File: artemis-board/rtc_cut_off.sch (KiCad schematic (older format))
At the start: 10 parts, among them Q1 2N7002, Q3 2N7002, U7 PCF8563T, U9 TCA6408A, Y2 32.768KHz

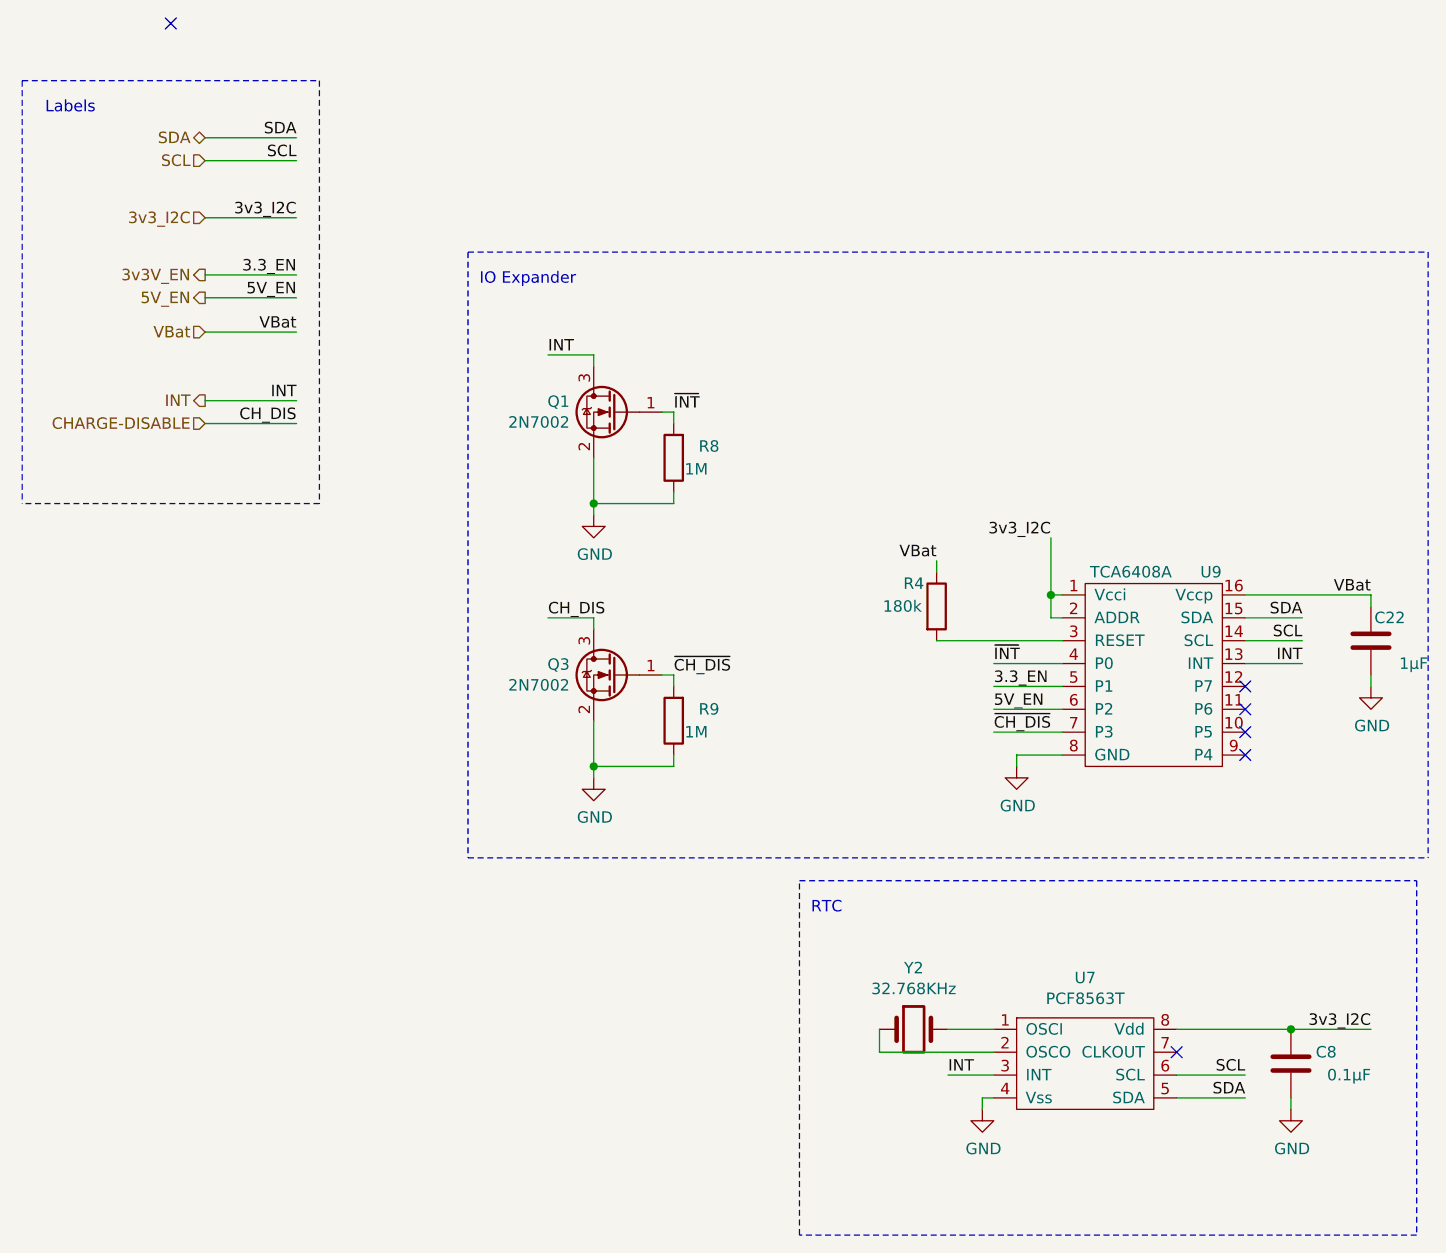
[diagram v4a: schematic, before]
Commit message: added cirquit to measure Vbat with esp in case of fuel gauge shortage
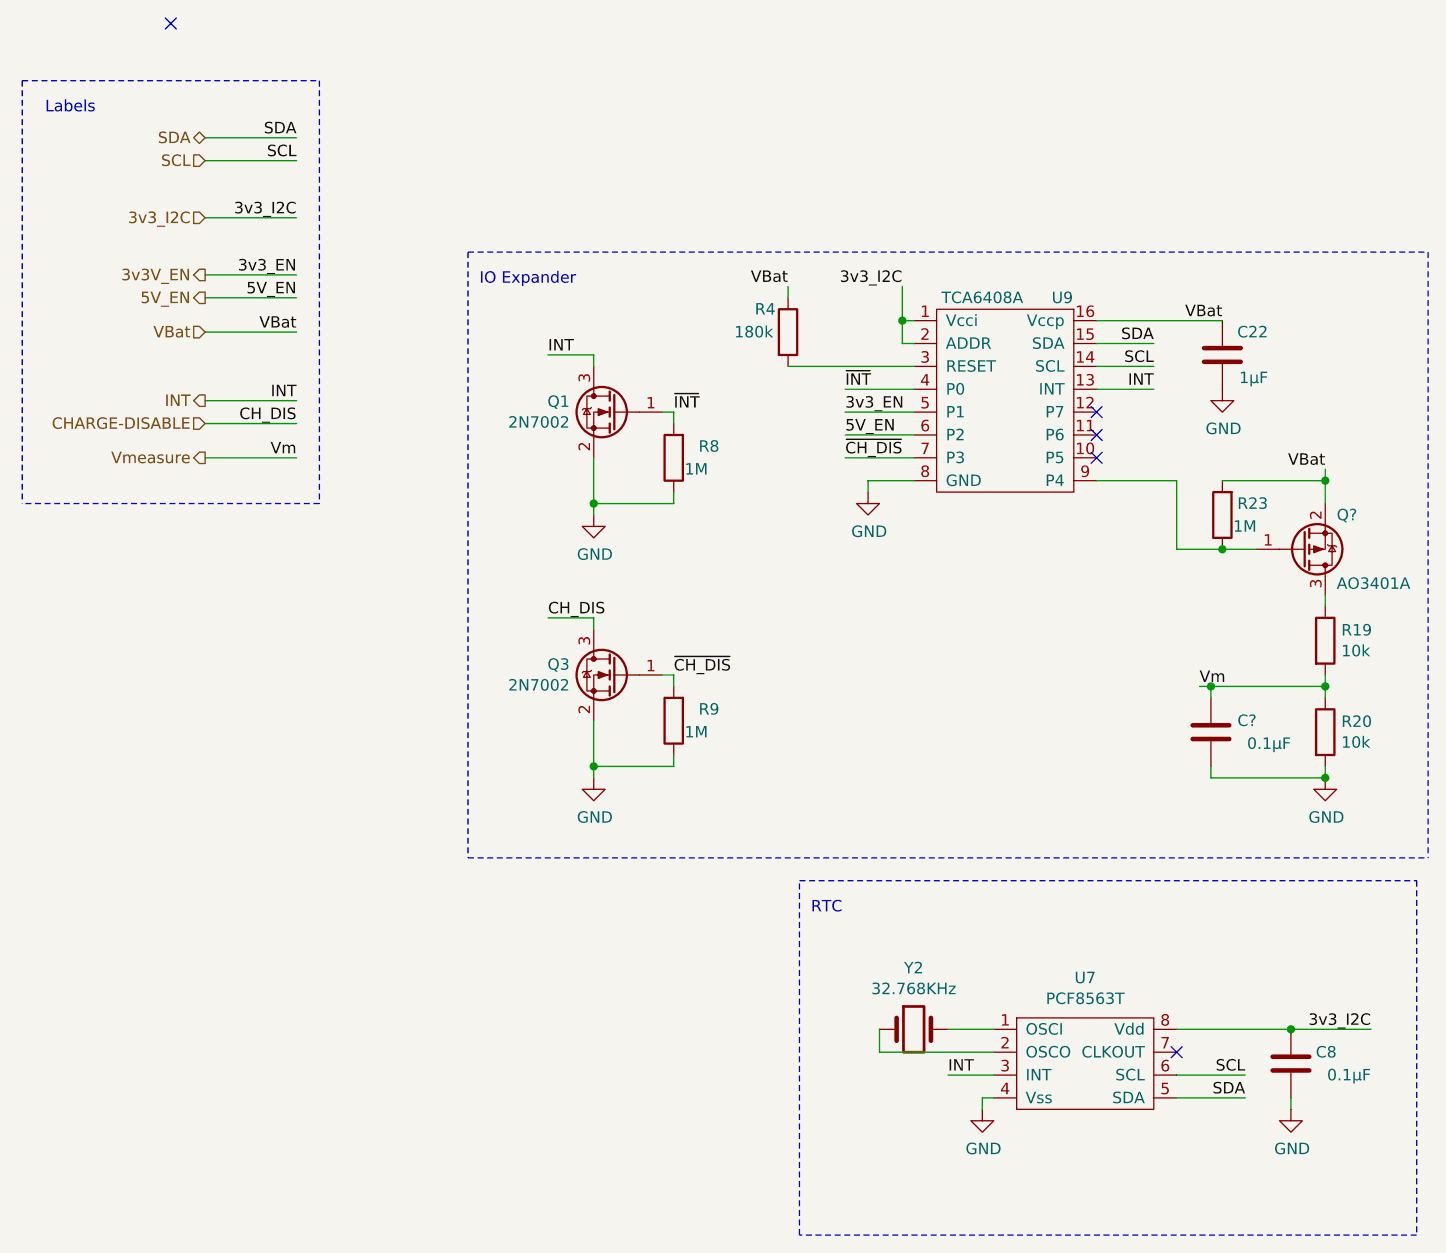
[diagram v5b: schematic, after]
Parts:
- added C?: 0.1µF, Capacitor_SMD:C_0603_1608Metric_Pad1.05x0.95mm_HandSolder, symbol Device:C
- added Q?: AO3401A, Package_TO_SOT_SMD:SOT-23_Handsoldering, symbol Transistor_FET:AO3401A
- added R19, R20: 10k, Resistor_SMD:R_0603_1608Metric_Pad1.05x0.95mm_HandSolder, symbol Device:R
- added R23: 1M, Resistor_SMD:R_0603_1608Metric_Pad1.05x0.95mm_HandSolder, symbol Device:R
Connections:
- net GND: now also C?.1, R20.2
- net VBat: now also Q?.2 (S), R23.2
- net at U9.9 (P4): now also Q?.1 (G), R23.1
- new net: Q?.3 (D), R19.1
- new net Vmeasure: C?.2, R19.2, R20.1
- no-connect marks 6 -> 5
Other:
- moved on the sheet: C22, R4, U9

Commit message: .
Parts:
- gave numbers to parts that had none: 1
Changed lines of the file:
@@
 Vm
 $Comp
-L Device:C C?
+L Device:C C26
 U 1 1 60A8251F
 P 5750 3450
-F 0 "C?" H 5550 3400 50  0000 L CNN
+F 0 "C26" H 5500 3400 50  0000 L CNN
 F 1 "0.1µF" H 5400 3500 50  0000 L CNN
 F 2 "Capacitor_SMD:C_0603_1608Metric_Pad1.05x0.95mm_HandSolder" H 5788 3300 50  0001 C CNN
